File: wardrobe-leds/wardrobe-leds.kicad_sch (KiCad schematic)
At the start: 47 parts, among them J1 LED strip, J2 LED strip, J3 LED strip, J4 LED strip, J5 Power, Q1 IRF540N, Q2 IRF540N, Q3 IRF540N, Q4 IRF540N, U1 LM339

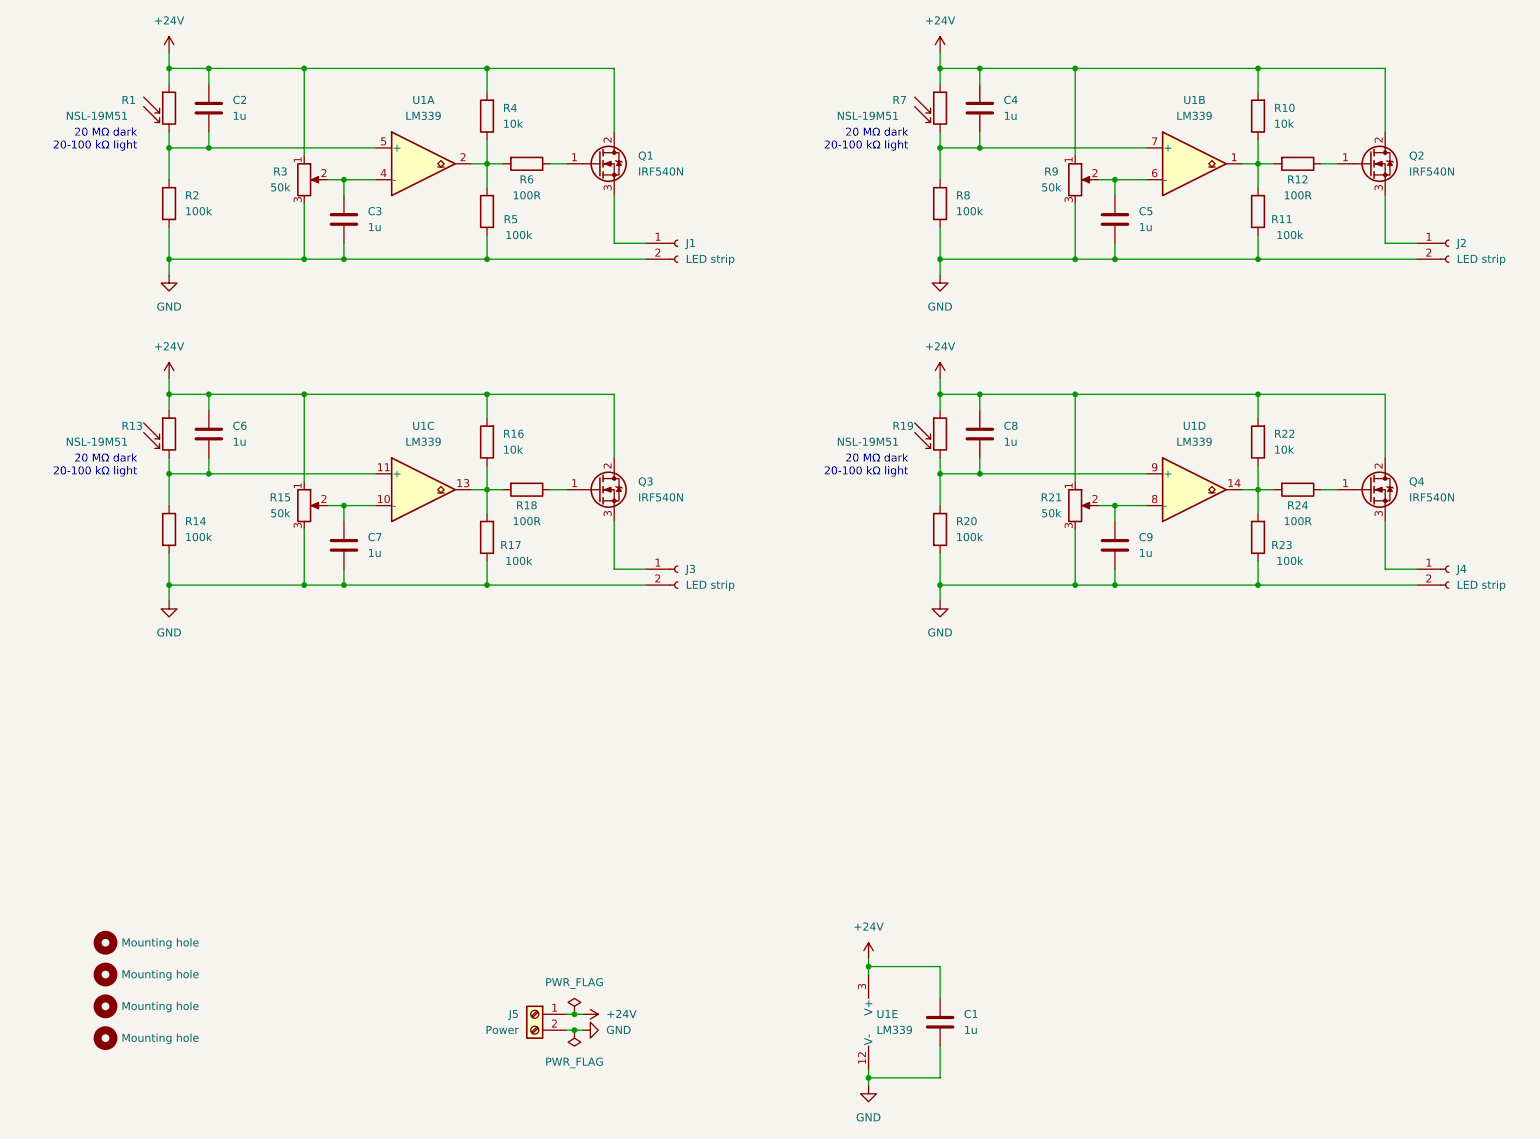
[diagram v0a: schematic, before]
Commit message: Update driver to use P-channel MOSFET to avoid Vgs voltage drop; add dimmer control; add hysteresis
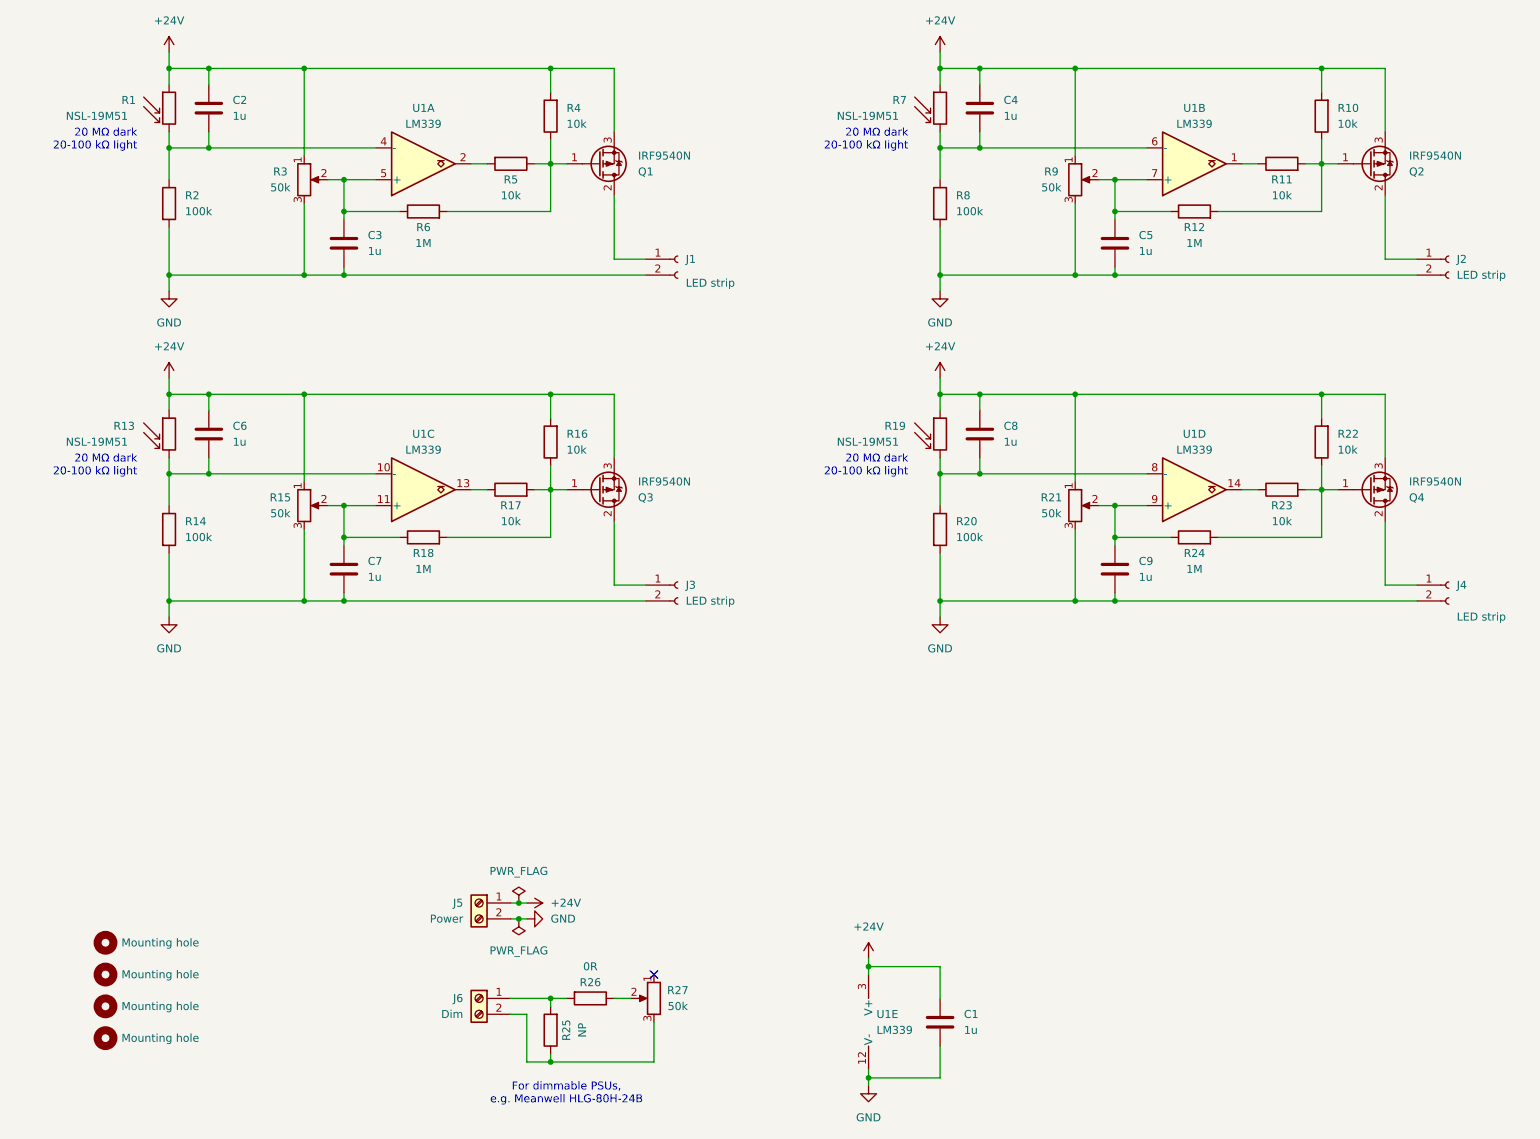
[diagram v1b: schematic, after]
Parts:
- removed Q1, Q2, Q3, Q4: IRF540N, Package_TO_SOT_THT:TO-220-3_Horizontal_TabDown, symbol Transistor_FET:IRF540N
- removed R5: 100k, Resistor_SMD:R_0805_2012Metric, symbol Device:R
- added J6: Dim, TerminalBlock_Phoenix:TerminalBlock_Phoenix_MKDS-3-2-5.08_1x02_P5.08mm_Horizontal, symbol Connector:Screw_Terminal_01x02
- added Q1, Q2, Q3, Q4: IRF9540N, Package_TO_SOT_THT:TO-220-3_Horizontal_TabDown, symbol Transistor_FET:IRF9540N
- added R25: NP, Resistor_SMD:R_0805_2012Metric, symbol Device:R
- added R26: 0R, Resistor_SMD:R_0805_2012Metric, symbol Device:R
- added R27: 50k, Potentiometer_SMD:Potentiometer_Bourns_3314J_Vertical, symbol Device:R_Potentiometer
- added R6: 1M, Resistor_SMD:R_0805_2012Metric, symbol Device:R
- R11, R17, R23: value 100k -> 10k
- R12, R18, R24: value 100R -> 1M
- R5: renamed from R6; value 100R -> 10k
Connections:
- net +24V: now also Q1.3 (S), Q2.3 (S), Q3.3 (S), Q4.3 (S)
- net GND: no longer R11.1, R17.1, R23.1
- net at C6.2, R13.2, R14.1: now also U1.10 (-); no longer U1.11 (+)
- net at R18.1: now also C7.1, R15.2, U1.11 (+)
- net at R16.1, R17.2, R18.2: now also Q3.1 (G); no longer U1.13
- net at R24.1: now also C9.1, R21.2, U1.9 (+)
- net at R22.1, R23.2, R24.2: now also Q4.1 (G); no longer U1.14
- net at R12.1: now also C5.1, R9.2, U1.7 (+)
- net at R10.1, R11.2, R12.2: now also Q2.1 (G); no longer U1.1
- net at C8.2, R19.2, R20.1: now also U1.8 (-); no longer U1.9 (+)
- net at C3.1, R3.2: now also U1.5 (+), R6.1; no longer U1.4 (-)
- net at C4.2, R7.2, R8.1: now also U1.6 (-); no longer U1.7 (+)
- net at J2.1 (Pin_1): now also Q2.2 (D)
- net at R5.2, U1.2: no longer R4.1
- net at R5.1: now also R4.1, Q1.1 (G), R6.2
- net at J1.1 (Pin_1): now also Q1.2 (D)
- net at C2.2, R1.2, R2.1: now also U1.4 (-); no longer U1.5 (+)
- net at J3.1 (Pin_1): now also Q3.2 (D)
- net at J4.1 (Pin_1): now also Q4.2 (D)
- new net: J6.1 (Pin_1), R25.2, R26.2
- new net: J6.2 (Pin_2), R25.1, R27.3
- new net: R26.1, R27.2
- new net: R11.1, U1.1
- new net: R17.1, U1.13
- new net: R23.1, U1.14
- no-connect marks 0 -> 1
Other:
- note added: "For dimmable PSUs, e.g. Meanwell HLG-80H-24B"
- moved on the sheet: C3, C5, C7, C9, J1, J2, J3, J4, J5, R10, R11, R16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
